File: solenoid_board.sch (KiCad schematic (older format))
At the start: 67 parts, among them J2 MCU_LEFT_LEGS, J3 MCU_RIGHT_LEGS

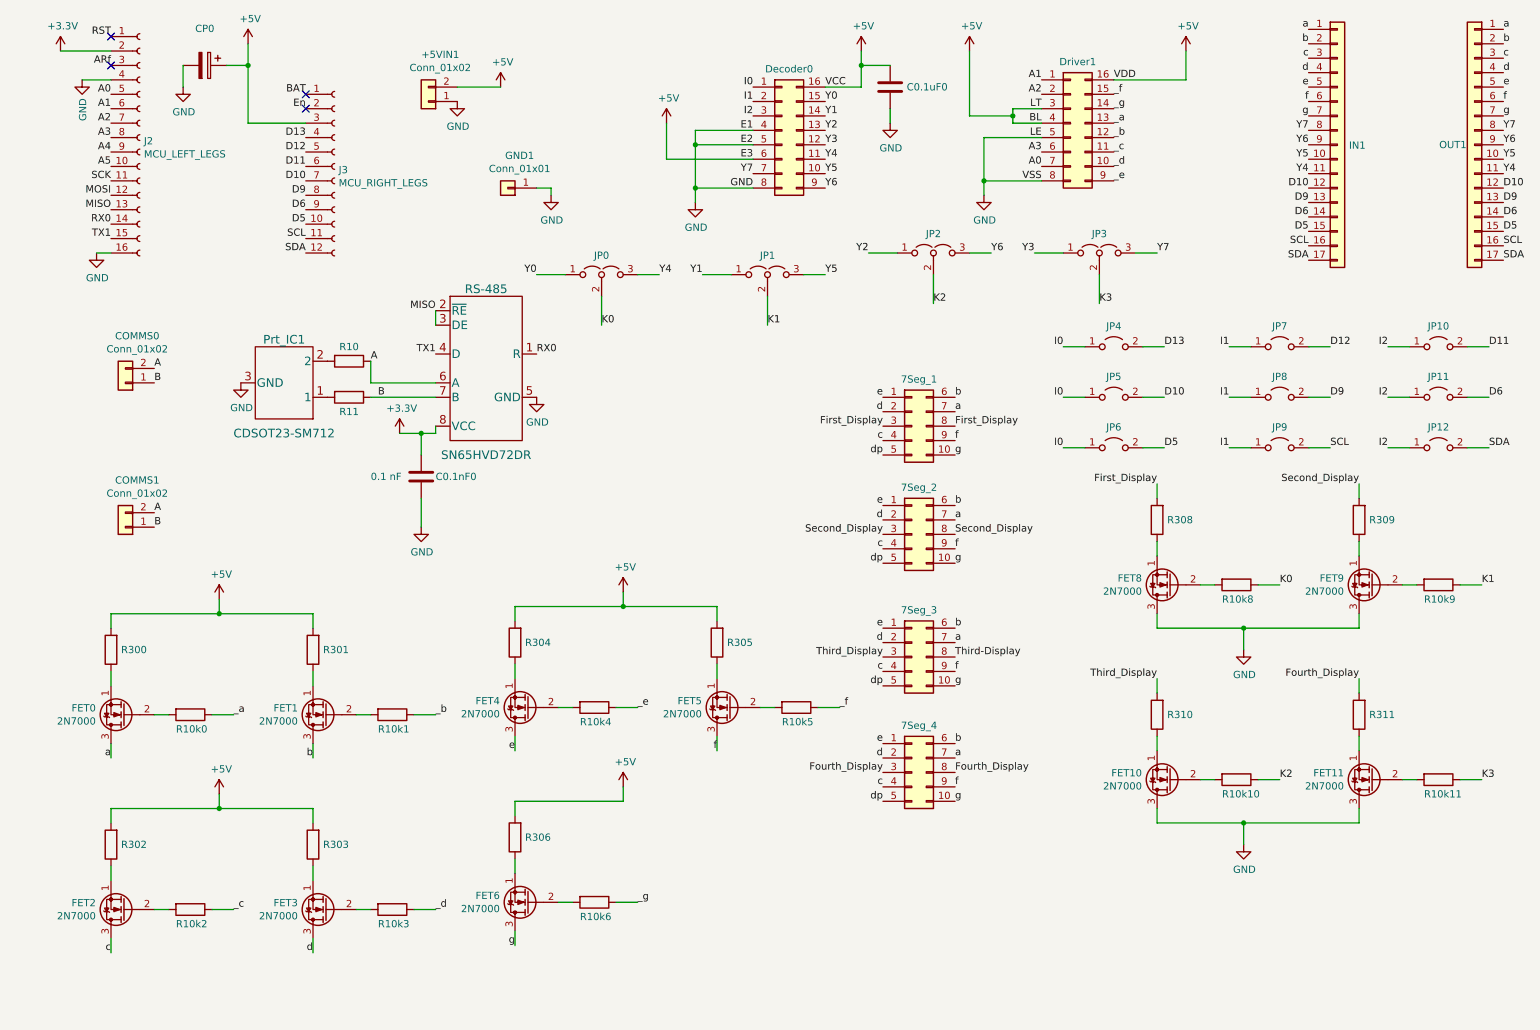
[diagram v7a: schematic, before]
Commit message: Revised Schematic based on Dr. Fuch's suggested edits. Need to finalize Geometry and update BOM.
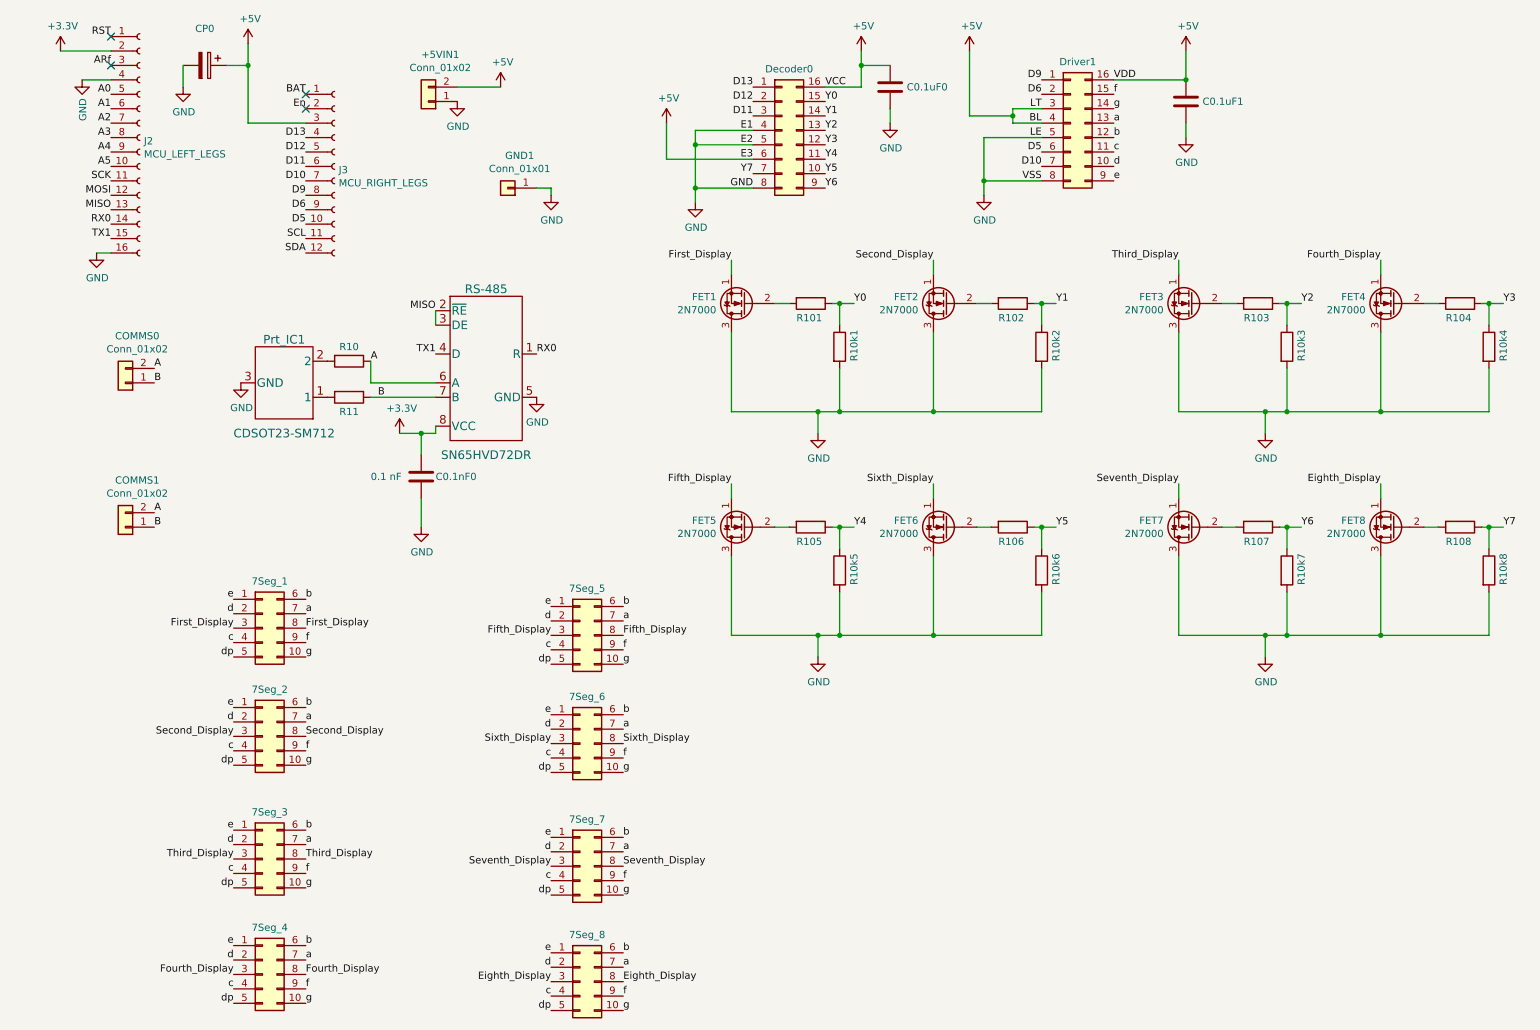
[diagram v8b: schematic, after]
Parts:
- removed FET0, FET10, FET11, FET9: 2N7000, Package_TO_SOT_THT:TO-92_Inline, symbol Transistor_FET:2N7000
- removed IN1, OUT1: Conn_01x17, Connector_PinHeader_2.54mm:PinHeader_1x17_P2.54mm_Vertical, symbol Connector_Generic:Conn_01x17
- removed JP0, JP1, JP2, JP3: Jumper_3_Open, Jumper:SolderJumper-3_P1.3mm_Open_RoundedPad1.0x1.5mm, symbol Jumper:Jumper_3_Open
- removed JP10, JP11, JP12, JP4, JP5, JP6, JP7, JP8, JP9: Jumper_2_Open, Jumper:SolderJumper-2_P1.3mm_Open_RoundedPad1.0x1.5mm, symbol Jumper:Jumper_2_Open
- removed R10k0, R10k10, R10k11, R10k9: 10k, Resistor_THT:R_Axial_DIN0204_L3.6mm_D1.6mm_P5.08mm_Vertical, symbol Device:R
- removed R300, R301, R302, R303, R304, R305, R306, R308, R309, R310, R311: 300, Resistor_THT:R_Axial_DIN0204_L3.6mm_D1.6mm_P5.08mm_Vertical, symbol Device:R
- added 7Seg_5, 7Seg_6, 7Seg_7, 7Seg_8: Conn_02x05_Top_Bottom, Kingbright_10-DinDisplay:SC10-21SRWA, symbol Connector_Generic:Conn_02x05_Top_Bottom
- added C0.1uF1: 0.1 uF, Capacitor_THT:CP_Radial_D4.0mm_P2.00mm, symbol Device:C
- added FET7: 2N7000, Package_TO_SOT_THT:TO-92_Inline, symbol Transistor_FET:2N7000
- added R101, R102, R103, R104, R105, R106, R107, R108: 100, Resistor_THT:R_Axial_DIN0204_L3.6mm_D1.6mm_P5.08mm_Vertical, symbol Device:R
- added R10k7: 10k, Resistor_THT:R_Axial_DIN0204_L3.6mm_D1.6mm_P5.08mm_Vertical, symbol Device:R
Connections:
- net I0 is gone; now on net D13: Decoder0.1 (Pin_1)
- net I1 is gone; now on net D12: Decoder0.2 (Pin_2)
- net I2 is gone; now on net D11: Decoder0.3 (Pin_3)
- net K0 is gone; now on net Y7: R10k8.1
- net Third-Display is gone; now on net Third_Display: 7Seg_3.8 (Pin_8)
- net _a is gone; now on net a: Driver1.13 (Pin_13)
- net +5V: now also C0.1uF1.1
- net A0: no longer Driver1.7 (Pin_7)
- net A1: no longer Driver1.1 (Pin_1)
- net A2: no longer Driver1.2 (Pin_2)
- net A3: no longer Driver1.6 (Pin_6)
- net D10: now also Driver1.7 (Pin_7)
- net D5: now also Driver1.6 (Pin_6)
- net D6: now also Driver1.2 (Pin_2)
- net D9: now also Driver1.1 (Pin_1)
- net First_Display: now also FET1.1 (S)
- net Fourth_Display: now also FET4.1 (S)
- net GND: now also FET1.3 (D), FET2.3 (D), FET3.3 (D), FET4.3 (D), FET5.3 (D), FET6.3 (D), R10k1.2, R10k2.2, R10k3.2, R10k4.2, R10k5.2, R10k6.2, R10k8.2, C0.1uF1.2, FET7.3 (D), R10k7.2
- net Second_Display: now also FET2.1 (S)
- net Third_Display: now also FET3.1 (S)
- net Y0: now also R10k1.1, R101.1
- net Y1: now also R10k2.1, R102.1
- net Y2: now also R10k3.1, R103.1
- net Y3: now also R10k4.1, R104.1
- net Y4: now also R10k5.1, R105.1
- net Y5: now also R10k6.1, R106.1
- net Y6: now also R107.1, R10k7.1
- net Y7: now also R108.1
- net a: now also 7Seg_5.7 (Pin_7), 7Seg_6.7 (Pin_7), 7Seg_7.7 (Pin_7), 7Seg_8.7 (Pin_7)
- net b: now also Driver1.12 (Pin_12), 7Seg_5.6 (Pin_6), 7Seg_6.6 (Pin_6), 7Seg_7.6 (Pin_6), 7Seg_8.6 (Pin_6); no longer FET1.3 (D)
- net c: now also Driver1.11 (Pin_11), 7Seg_5.4 (Pin_4), 7Seg_6.4 (Pin_4), 7Seg_7.4 (Pin_4), 7Seg_8.4 (Pin_4); no longer FET2.3 (D)
- net d: now also Driver1.10 (Pin_10), 7Seg_5.2 (Pin_2), 7Seg_6.2 (Pin_2), 7Seg_7.2 (Pin_2), 7Seg_8.2 (Pin_2); no longer FET3.3 (D)
- net dp: now also 7Seg_5.5 (Pin_5), 7Seg_6.5 (Pin_5), 7Seg_7.5 (Pin_5), 7Seg_8.5 (Pin_5)
- net e: now also Driver1.9 (Pin_9), 7Seg_5.1 (Pin_1), 7Seg_6.1 (Pin_1), 7Seg_7.1 (Pin_1), 7Seg_8.1 (Pin_1); no longer FET4.3 (D)
- net f: now also Driver1.15 (Pin_15), 7Seg_5.9 (Pin_9), 7Seg_6.9 (Pin_9), 7Seg_7.9 (Pin_9), 7Seg_8.9 (Pin_9); no longer FET5.3 (D)
- net g: now also Driver1.14 (Pin_14), 7Seg_5.10 (Pin_10), 7Seg_6.10 (Pin_10), 7Seg_7.10 (Pin_10), 7Seg_8.10 (Pin_10); no longer FET6.3 (D)
- net at FET1.2 (G): now also R101.2; no longer R10k1.2
- net at FET2.2 (G): now also R102.2; no longer R10k2.2
- net at FET3.2 (G): now also R103.2; no longer R10k3.2
- net at FET4.2 (G): now also R104.2; no longer R10k4.2
- net Fifth_Display: now reaches FET5.1 (S)
- net Fifth_Display: now also 7Seg_5.3 (Pin_3), 7Seg_5.8 (Pin_8)
- net at FET5.2 (G): now also R105.2; no longer R10k5.2
- net Sixth_Display: now reaches FET6.1 (S)
- net Sixth_Display: now also 7Seg_6.3 (Pin_3), 7Seg_6.8 (Pin_8)
- net at FET6.2 (G): now also R106.2; no longer R10k6.2
- net Eighth_Display: now reaches FET8.1 (S)
- net Eighth_Display: now also 7Seg_8.3 (Pin_3), 7Seg_8.8 (Pin_8)
- net at FET8.2 (G): now also R108.2; no longer R10k8.2
- removed net _b: Driver1.12 (Pin_12), R10k1.1
- removed net _c: Driver1.11 (Pin_11), R10k2.1
- removed net _d: Driver1.10 (Pin_10), R10k3.1
- removed net _e: Driver1.9 (Pin_9), R10k4.1
- removed net _f: Driver1.15 (Pin_15), R10k5.1
- removed net _g: Driver1.14 (Pin_14), R10k6.1
- new net: FET7.2 (G), R107.2
- new net Seventh_Display: 7Seg_7.3 (Pin_3), 7Seg_7.8 (Pin_8), FET7.1 (S)
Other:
- moved on the sheet: 7Seg_1, 7Seg_2, 7Seg_3, 7Seg_4
